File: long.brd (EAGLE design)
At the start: 20 x 60 mm, 20 parts, among them U1 USD-SOCKET, U2 MCP73831, U3 TPS61200, X1 Micro USB

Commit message: Added round boards
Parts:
- added E$1: (no value), microbuilder:UG-2832HSWEG02_WRAPUNDER
- added JP1, JP2, JP3, JP4, JP5, JP6, JP8, JP9: (no value), pinhead:1X04
- added U$2: UBLOX_MAX, Ava:UBLOX_MAX
- added U$3: ADXL377, SparkFun-Sensors:LFCSP_LQ-16
- moved U1 5.10 mm to (3.00, 49.2)
- moved U$1 1.43 mm to (6.50, 30.9)
- moved JP7 0.50 mm to (10.3, 12.1)
- moved R6 0.10 mm to (18.6, 13.9)
- moved R7 0.10 mm to (16.3, 13.9)
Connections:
- new net 10_GND: U$2.10_GND
- new net 12_GND: U$2.12_GND
- new net 1_GND: U$2.1_GND
- new net 7_VCC_IO: U$2.7_VCC_IO
- new net 8_VCC: U$2.8_VCC
- new net 9_V_RESET: U$2.9_V_RESET
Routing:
- net GND: track 35.4 -> 34.3 mm
- net UVLO: track 25.8 -> 25.2 mm
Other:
- board size 20 x 60 mm -> 43.8 x 65.1 mm

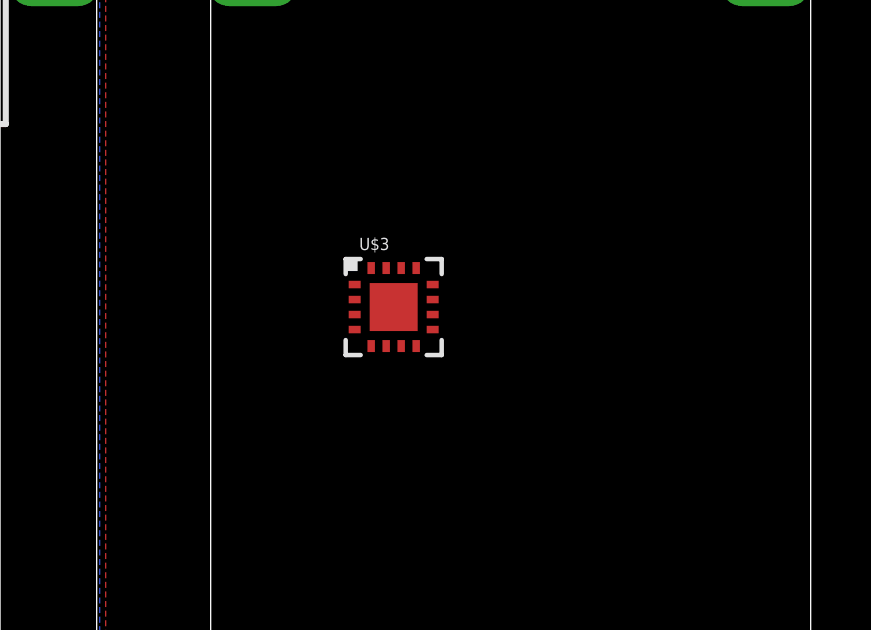
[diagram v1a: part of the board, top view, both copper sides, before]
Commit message: Added ADXL375 library
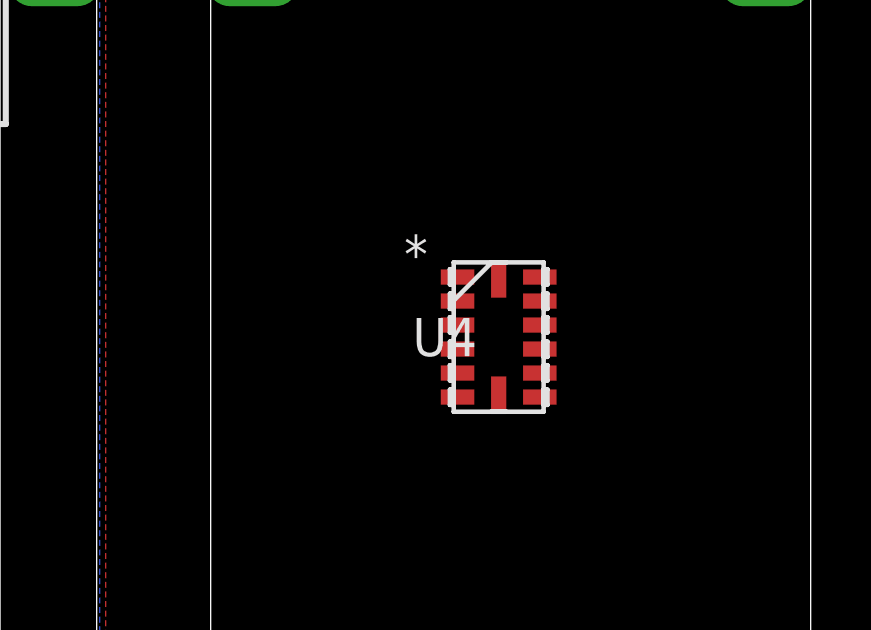
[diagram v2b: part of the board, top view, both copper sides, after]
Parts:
- removed U$3: ADXL377, SparkFun-Sensors:LFCSP_LQ-16
- added U4: ADXL375BCCZ, adxl375bccz:LGA_CC-14-1
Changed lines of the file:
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@@
 <element name="JP8" library="pinhead" package="1X04" value="" x="25.2" y="57.7" rot="MR90"/>
 <element name="JP9" library="pinhead" package="1X04" value="" x="42.3" y="57.7" rot="MR90"/>
-<element name="U$3" library="SparkFun-Sensors" package="LFCSP_LQ-16" value="ADXL377" x="29.9" y="43.1"/>
 <element name="E$1" library="microbuilder" package="UG-2832HSWEG02_WRAPUNDER" value="" x="10" y="45.9" rot="MR90"/>
+<element name="U4" library="adxl375bccz" package="LGA_CC-14-1" value="ADXL375BCCZ" x="33.4" y="42.1"/>
 </elements>
 <signals>
